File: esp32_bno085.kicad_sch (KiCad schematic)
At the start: 36 parts, among them J1 530480210, J2 USB_C_Receptacle_USB2.0_16P, Q1 AO3401A, SW1 RESET, SW2 BOOT, U1 TP4056-42-ESOP8, U2 ESP32-S3-WROOM-1, U3 BNO085, U4 XC6220B331MR, Y1 32.7680kHz

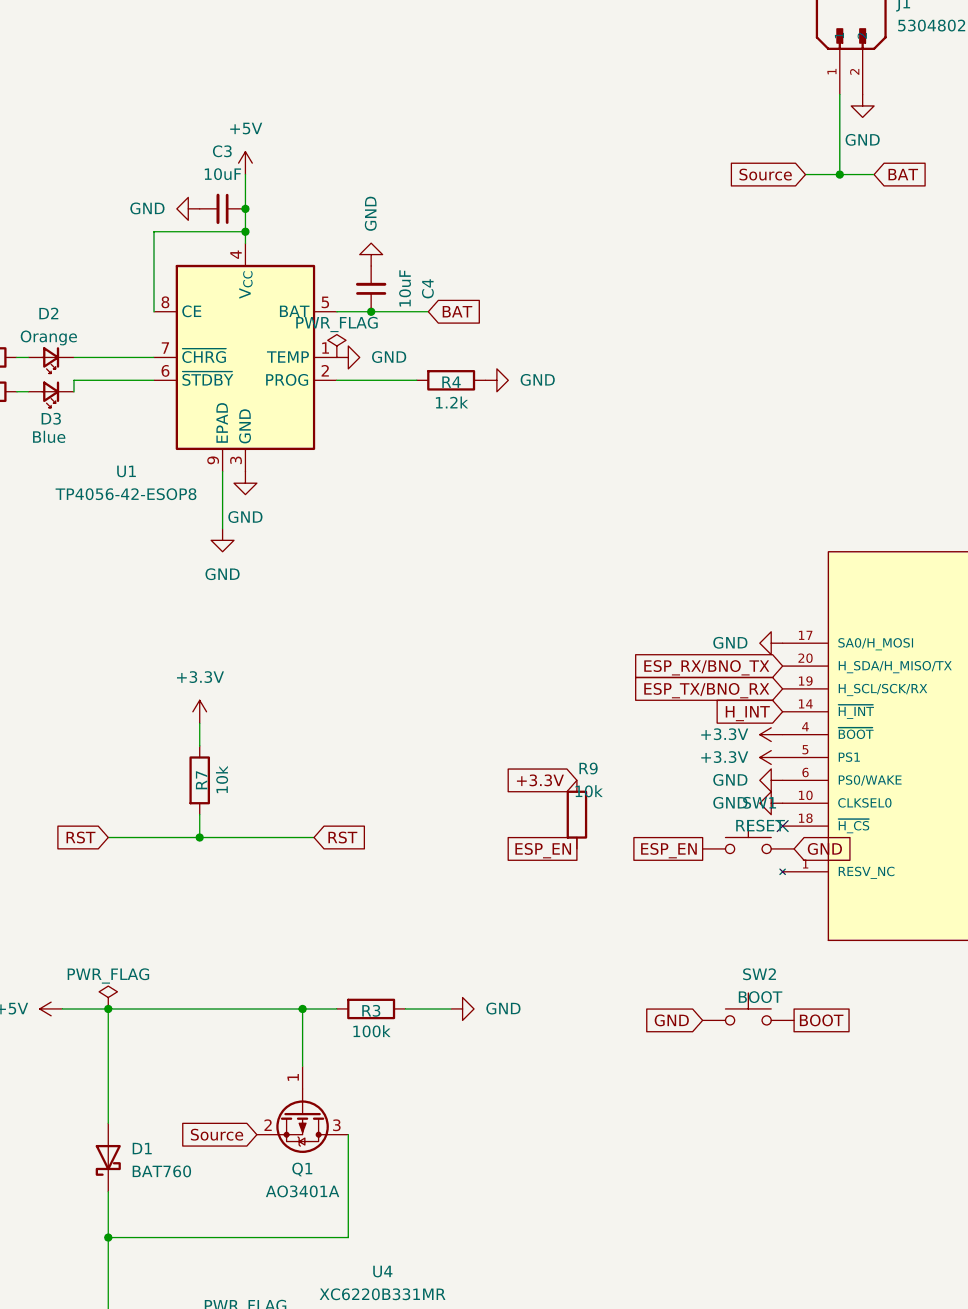
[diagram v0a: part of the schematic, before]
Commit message: Clean up KiCad schematic ERC warnings
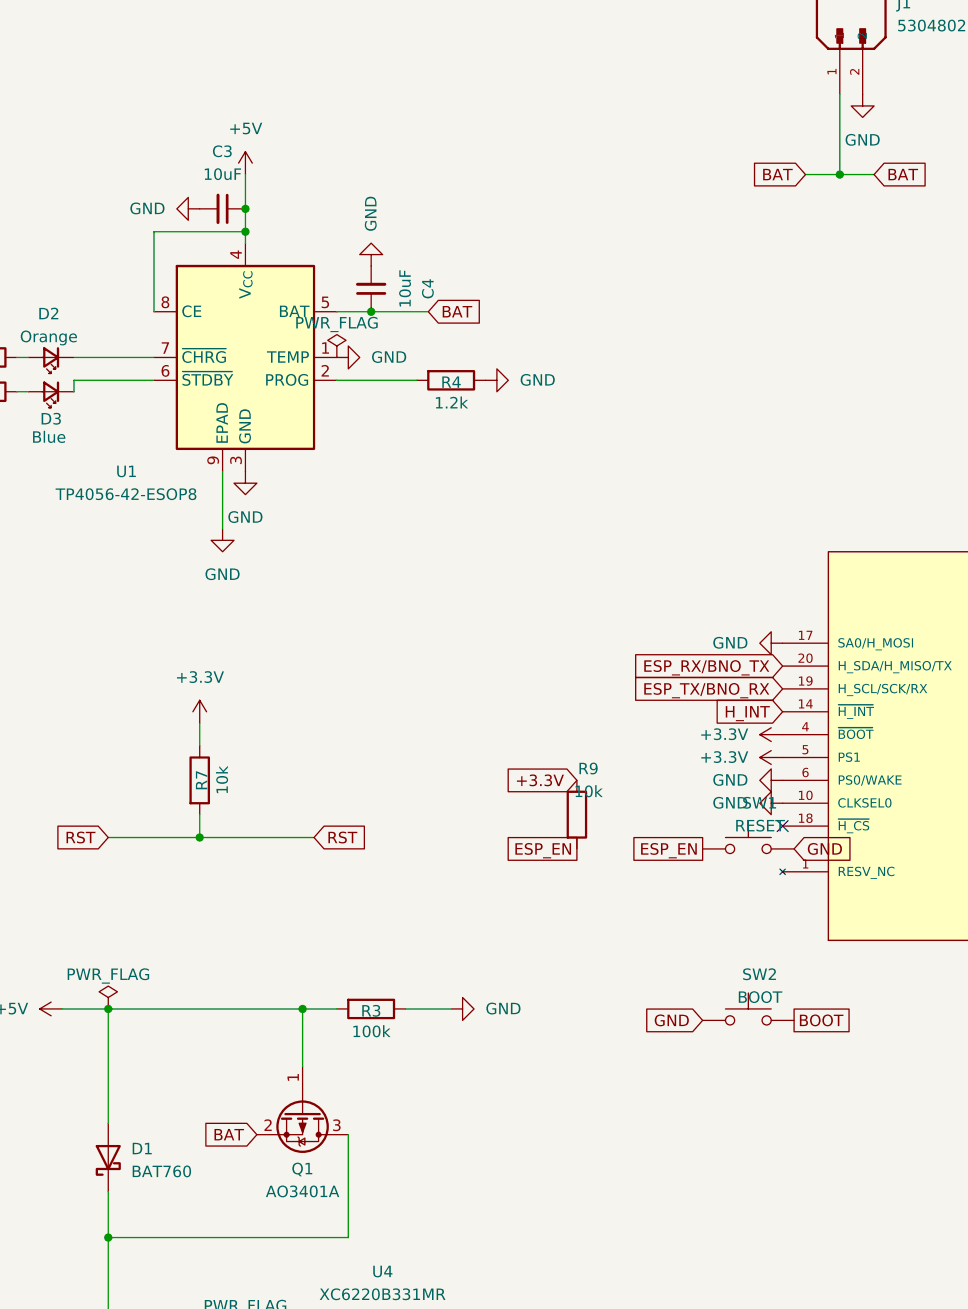
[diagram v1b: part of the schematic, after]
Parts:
- J2: symbol Connector:USB_C_Receptacle_USB2.0_16P -> USB_C_HRO:USB_C_Receptacle_USB2.0_16P
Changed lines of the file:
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@@
 		)
 	)
-	(global_label "Source"
+	(global_label "BAT"
 		(shape input)
 		(at 172.72 40.64 180)
@@
 		)
 	)
-	(global_label "Source"
+	(global_label "BAT"
 		(shape input)
 		(at 111.76 147.32 180)
@@
 	)
 	(symbol
-		(lib_id "Connector:USB_C_Receptacle_USB2.0_16P")
+		(lib_id "USB_C_HRO:USB_C_Receptacle_USB2.0_16P")
 		(at 31.75 41.91 0)
 		(unit 1)

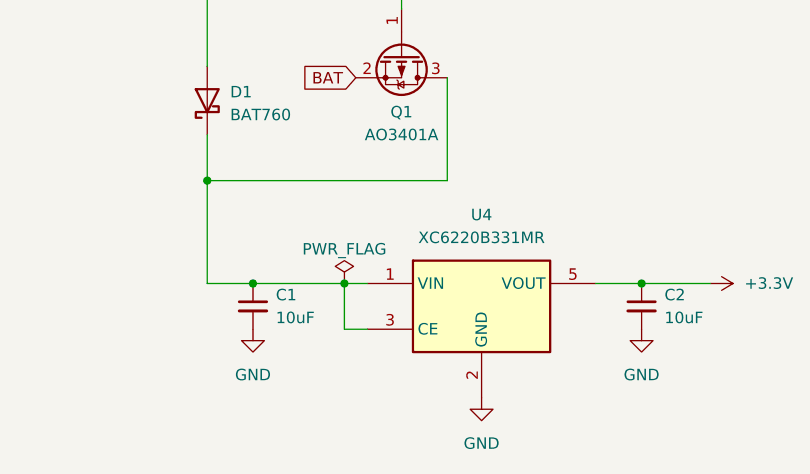
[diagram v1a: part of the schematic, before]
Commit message: Clarify VSYS rail and JLCPCB order notes
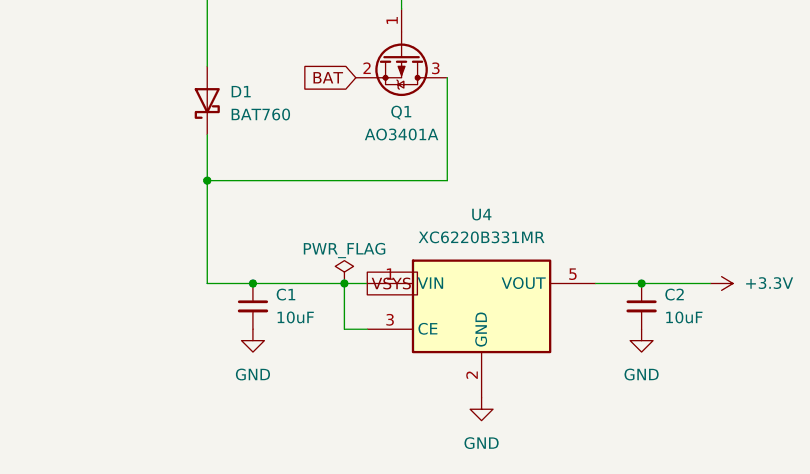
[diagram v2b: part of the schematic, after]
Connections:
- net VSYS: now reaches C1.1, D1.1 (K), Q1.3 (D), U4.1 (VIN), U4.3 (CE)
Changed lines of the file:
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@@
+		)
+	)
+	(global_label "VSYS"
+		(shape passive)
+		(at 113.03 170.18 0)
+		(fields_autoplaced yes)
+		(effects
+			(font
+				(size 1.27 1.27)
+			)
+			(justify left)
+		)
+		(property "Intersheetrefs" "${INTERSHEET_REFS}"
+			(at 121.03 170.18 0)
+			(effects
+				(font
+					(size 1.27 1.27)
+				)
+				(justify left)
+				(hide yes)
+			)
 		)
 	)

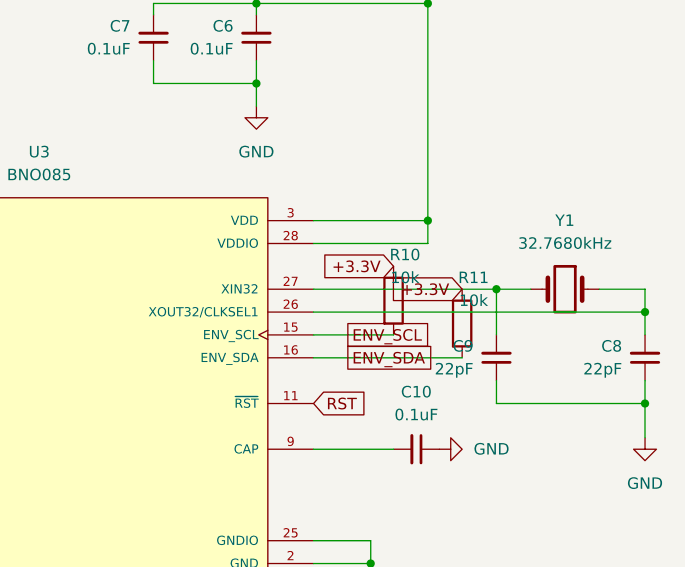
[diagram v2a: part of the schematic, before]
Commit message: Clarify DRC checks and BNO crystal routing
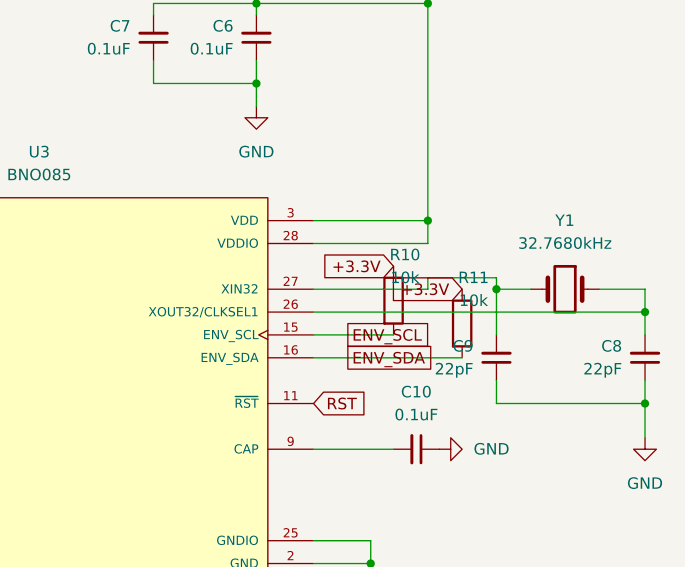
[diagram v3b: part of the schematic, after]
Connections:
- net +3.3V: no longer C9.2, U3.27 (XIN32), Y1.2
- new net: C9.2, U3.27 (XIN32), Y1.2
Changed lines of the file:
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@@
 	(wire
 		(pts
-			(xy 251.46 92.71) (xy 231.14 92.71)
+			(xy 231.14 92.71) (xy 243.84 92.71)
 		)
 		(stroke
+			(width 0)
+			(type default)
+		)
+	)
+	(wire
+		(pts
+			(xy 243.84 92.71) (xy 243.84 91.44)
+		)
+		(stroke
+			(width 0)
+			(type default)
+		)
+	)
+	(wire
+		(pts
+			(xy 243.84 91.44) (xy 251.46 91.44)
+		)
+		(stroke
+			(width 0)
+			(type default)
+		)
+	)
+	(wire
+		(pts
+			(xy 251.46 91.44) (xy 251.46 92.71)
+		)
+		(stroke

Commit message: Add JLCPCB BOM metadata fields
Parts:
- D1: LCSC (none) -> C124187; MPN (none) -> BAT760-7; Manufacturer (none) -> DIODES
- J1: BOM Comments (none) -> Through-hole battery header; confirm Standard PCBA support 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; LCSC (none) -> C505099; MPN (none) -> 530480210; Manufacturer (none) -> Molex
- J2: LCSC (none) -> C165948; MPN (none) -> TYPE-C-31-M-12; Manufacturer (none) -> Korean Hroparts Elec
- Q1: LCSC (none) -> C15127; MPN (none) -> AO3401A; Manufacturer (none) -> Alpha & Omega Semicon
- U1: LCSC (none) -> C16581; MPN (none) -> TP4056-42-ESOP8; Manufacturer (none) -> TOPPOWER(Nanjing Extension Microelectronics)
- U3: BOM Comments (none) -> LCSC page showed this part out of stock on 2026-07-13; veri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; LCSC (none) -> C5189642; MPN (none) -> BNO085; Manufacturer (none) -> CEVA
- U4: LCSC (none) -> C86534; MPN (none) -> XC6220B331MR-G; Manufacturer (none) -> Torex Semicon
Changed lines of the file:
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@@
 			)
 		)
+		(property "MPN" "AO3401A"
+			(at 116.84 144.78 0)
+			(effects
+				(font
+					(size 1.27 1.27)
+				)
+				(hide yes)
+			)
+		)
+		(property "Manufacturer" "Alpha & Omega Semicon"
+			(at 116.84 144.78 0)
+			(effects
+				(font
+					(size 1.27 1.27)
+				)
+				(hide yes)
+			)
+		)
+		(property "LCSC" "C15127"
+			(at 116.84 144.78 0)
+			(effects
+				(font
+					(size 1.27 1.27)
+				)
+				(hide yes)
+			)
+		)
 		(pin "1"
 		)
@@
 			)
 		)
+		(property "MPN" "TP4056-42-ESOP8"
+			(at 110.998 81.28 0)
+			(effects
+				(font
+					(size 1.27 1.27)
+				)
+				(hide yes)
+			)
+		)
+		(property "Manufacturer" "TOPPOWER(Nanjing Extension Microelectronics)"
+			(at 110.998 81.28 0)
+			(effects
+				(font
+					(size 1.27 1.27)
+				)
+				(hide yes)
+			)
+		)
+		(property "LCSC" "C16581"
+			(at 110.998 81.28 0)
+			(effects
+				(font
+					(size 1.27 1.27)
+				)
+				(hide yes)
+			)
+		)
 		(pin "8"
 		)
@@
 			)
 		)
+		(property "MPN" "BAT760-7"
+			(at 95.25 149.86 0)
+			(effects
+				(font
+					(size 1.27 1.27)
+				)
+				(hide yes)
+			)
+		)
+		(property "Manufacturer" "DIODES"
+			(at 95.25 149.86 0)
+			(effects
+				(font
+					(size 1.27 1.27)
+				)
+				(hide yes)
+			)
+		)
+		(property "LCSC" "C124187"
+			(at 95.25 149.86 0)
+			(effects
+				(font
+					(size 1.27 1.27)
+				)
+				(hide yes)
+			)
+		)
 		(pin "2"
 		)
@@
 			)
 		)
+		(property "MPN" "530480210"
+			(at 176.53 26.67 0)
+			(effects
+				(font
+					(size 1.27 1.27)
+				)
+				(justify bottom)
+				(hide yes)
+			)
+		)
+		(property "Manufacturer" "Molex"
+			(at 176.53 26.67 0)
+			(effects
+				(font
+					(size 1.27 1.27)
+				)
+				(justify bottom)
+				(hide yes)
+			)
+		)
+		(property "LCSC" "C505099"
+			(at 176.53 26.67 0)
+			(effects
+				(font
+					(size 1.27 1.27)
+				)
+				(justify bottom)
+				(hide yes)
+			)
+		)
+		(property "BOM Comments" "Through-hole battery header; confirm Standard PCBA support or hand-solder plan."
+			(at 176.53 26.67 0)
+			(effects
+				(font
+					(size 1.27 1.27)
+				)
+				(justify bottom)
+				(hide yes)
+			)
+		)
 		(property "Availability" "In Stock"
 			(at 176.53 26.67 0)
@@
 			)
 		)
+		(property "MPN" "BNO085"
+			(at 200.66 102.87 0)
+			(effects
+				(font
+					(size 1.27 1.27)
+				)
+				(justify bottom)
+				(hide yes)
+			)
+		)
+		(property "Manufacturer" "CEVA"
+			(at 200.66 102.87 0)
+			(effects
+				(font
+					(size 1.27 1.27)
+				)
+				(justify bottom)
+				(hide yes)
+			)
+		)
+		(property "LCSC" "C5189642"
+			(at 200.66 102.87 0)
+			(effects
+				(font
+					(size 1.27 1.27)
+				)
+				(justify bottom)
+				(hide yes)
+			)
+		)
+		(property "BOM Comments" "LCSC page showed this part out of stock on 2026-07-13; verify JLCPCB pre-order/availability before PCBA."
+			(at 200.66 102.87 0)
+			(effects
+				(font
+					(size 1.27 1.27)
+				)
+				(justify bottom)
+				(hide yes)
+			)
+		)
 		(property "Availability" "In Stock"
 			(at 200.66 102.87 0)
@@
 			)
 		)
+		(property "MPN" "TYPE-C-31-M-12"
+			(at 31.75 41.91 0)
+			(effects
+				(font
+					(size 1.27 1.27)
+				)
+				(hide yes)
+			)
+		)
+		(property "Manufacturer" "Korean Hroparts Elec"
+			(at 31.75 41.91 0)
+			(effects
+				(font
+					(size 1.27 1.27)
+				)
+				(hide yes)
+			)
+		)
+		(property "LCSC" "C165948"
+			(at 31.75 41.91 0)
+			(effects
+				(font
+					(size 1.27 1.27)
+				)
+				(hide yes)
+			)
+		)
 		(pin "A7"
 		)
@@
 			(at 125.73 172.72 0)
 			(effects
+				(font
+					(size 1.27 1.27)
+				)
+				(hide yes)
+			)
+		)
+		(property "MPN" "XC6220B331MR-G"
+			(at 125.73 172.72 0)
+			(effects
+				(font
+					(size 1.27 1.27)
+				)
+				(hide yes)
+			)
+		)
+		(property "Manufacturer" "Torex Semicon"
+			(at 125.73 172.72 0)
+			(effects
+				(font
+					(size 1.27 1.27)
+				)
+				(hide yes)
+			)
+		)
+		(property "LCSC" "C86534"
+			(at 125.73 172.72 0)
+			(effects

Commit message: Clarify stock scope and add PCB fiducials
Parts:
- U3: BOM Comments LCSC page showed this part out of stock on 2026-07-13; veri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 -> Lab inventory available per user; stock verification intent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
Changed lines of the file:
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@@
 			)
 		)
-		(property "BOM Comments" "LCSC page showed this part out of stock on 2026-07-13; verify JLCPCB pre-order/availability before PCBA."
+		(property "BOM Comments" "Lab inventory available per user; stock verification intentionally skipped. If using JLC-sourced turnkey PCBA, re-check C5189642 availability."
 			(at 200.66 102.87 0)
 			(effects

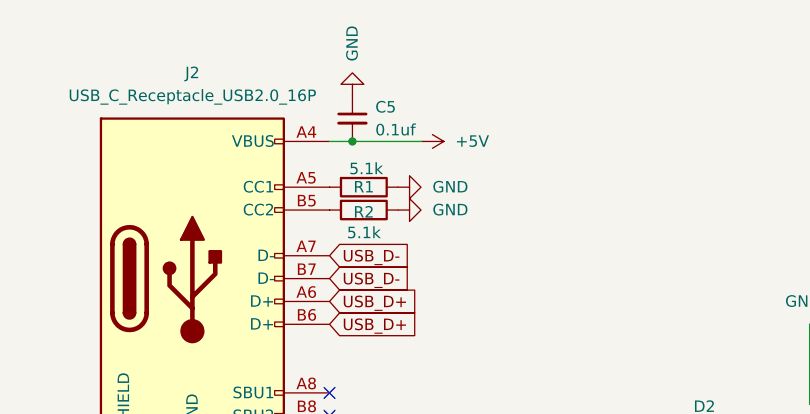
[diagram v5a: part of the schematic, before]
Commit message: Normalize capacitor BOM value and refresh JLC notes
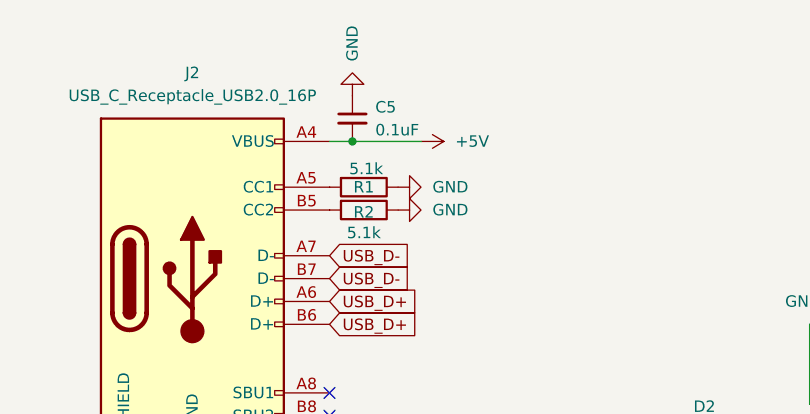
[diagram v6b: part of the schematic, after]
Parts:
- C5: value 0.1uf -> 0.1uF
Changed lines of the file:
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@@
 			)
 		)
-		(property "Value" "0.1uf"
+		(property "Value" "0.1uF"
 			(at 52.07 25.4062 0)
 			(effects

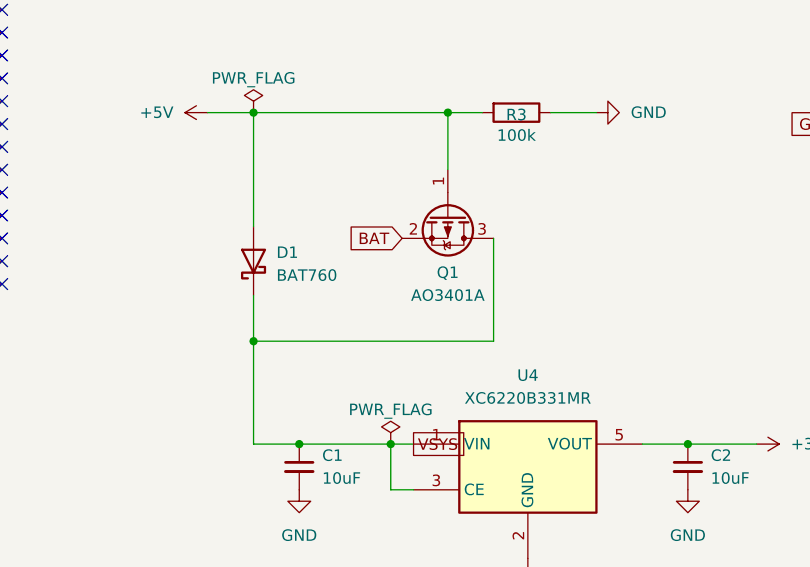
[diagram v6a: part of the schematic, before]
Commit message: Fix Q1 power path orientation
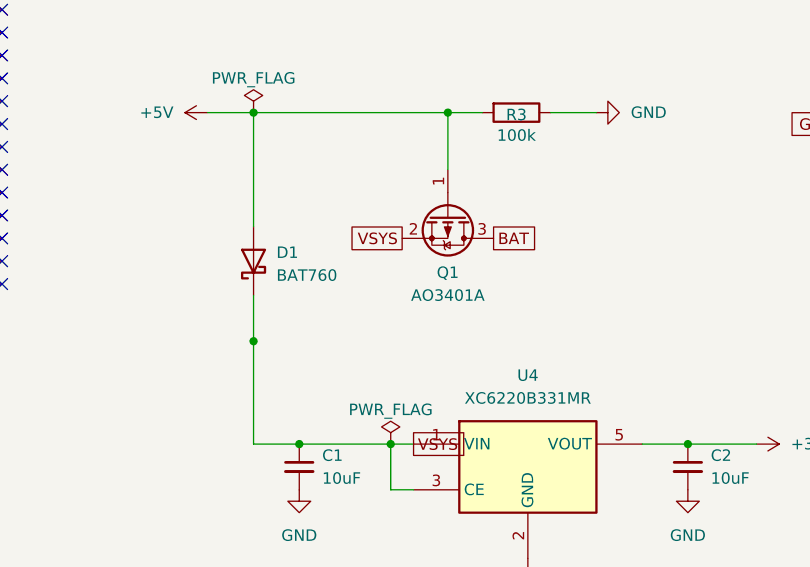
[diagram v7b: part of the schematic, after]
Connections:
- net BAT: now also Q1.3 (D); no longer Q1.2 (S)
- net VSYS: now also Q1.2 (S); no longer Q1.3 (D)
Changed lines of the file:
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@@
-	(wire
-		(pts
-			(xy 121.92 147.32) (xy 121.92 158.75)
-		)
-		(stroke
-			(width 0)
-			(type default)
-		)
-	)
 	(wire
 		(pts
@@
 	(wire
 		(pts
-			(xy 121.92 158.75) (xy 95.25 158.75)
-		)
-		(stroke
-			(width 0)
-			(type default)
-		)
-	)
-	(wire
-		(pts
 			(xy 95.25 133.35) (xy 95.25 146.05)
 		)
@@
 		)
 	)
+	(global_label "VSYS"
+		(shape passive)
+		(at 111.76 147.32 180)
+		(fields_autoplaced yes)
+		(effects
+			(font
+				(size 1.27 1.27)
+			)
+			(justify right)
+		)
+		(property "Intersheetrefs" "${INTERSHEET_REFS}"
+			(at 101.0936 147.32 0)
+			(effects
+				(font
+					(size 1.27 1.27)
+				)
+				(justify right)
+				(hide yes)
+			)
+		)
+	)
 	(global_label "BAT"
-		(shape input)
-		(at 111.76 147.32 180)
-		(fields_autoplaced yes)
-		(effects
-			(font
-				(size 1.27 1.27)
-			)
-			(justify right)
-		)
-		(property "Intersheetrefs" "${INTERSHEET_REFS}"
-			(at 102.3039 147.32 0)
-			(effects
-				(font
-					(size 1.27 1.27)
-				)
-				(justify right)
-				(hide yes)
-			)
+		(shape passive)
+		(at 121.92 147.32 0)
+		(fields_autoplaced yes)
+		(effects
+			(font
+				(size 1.27 1.27)
+			)
+			(justify left)
+		)
+		(property "Intersheetrefs" "${INTERSHEET_REFS}"
+			(at 128.2314 147.32 0)
+			(effects
+				(font
+					(size 1.27 1.27)
+				)
+				(justify left)
+				(hide yes)
+			)
